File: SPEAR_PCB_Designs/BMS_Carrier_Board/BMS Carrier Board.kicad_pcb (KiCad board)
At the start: 2 copper layers, 2 parts, among them U1 74LV1T08GW

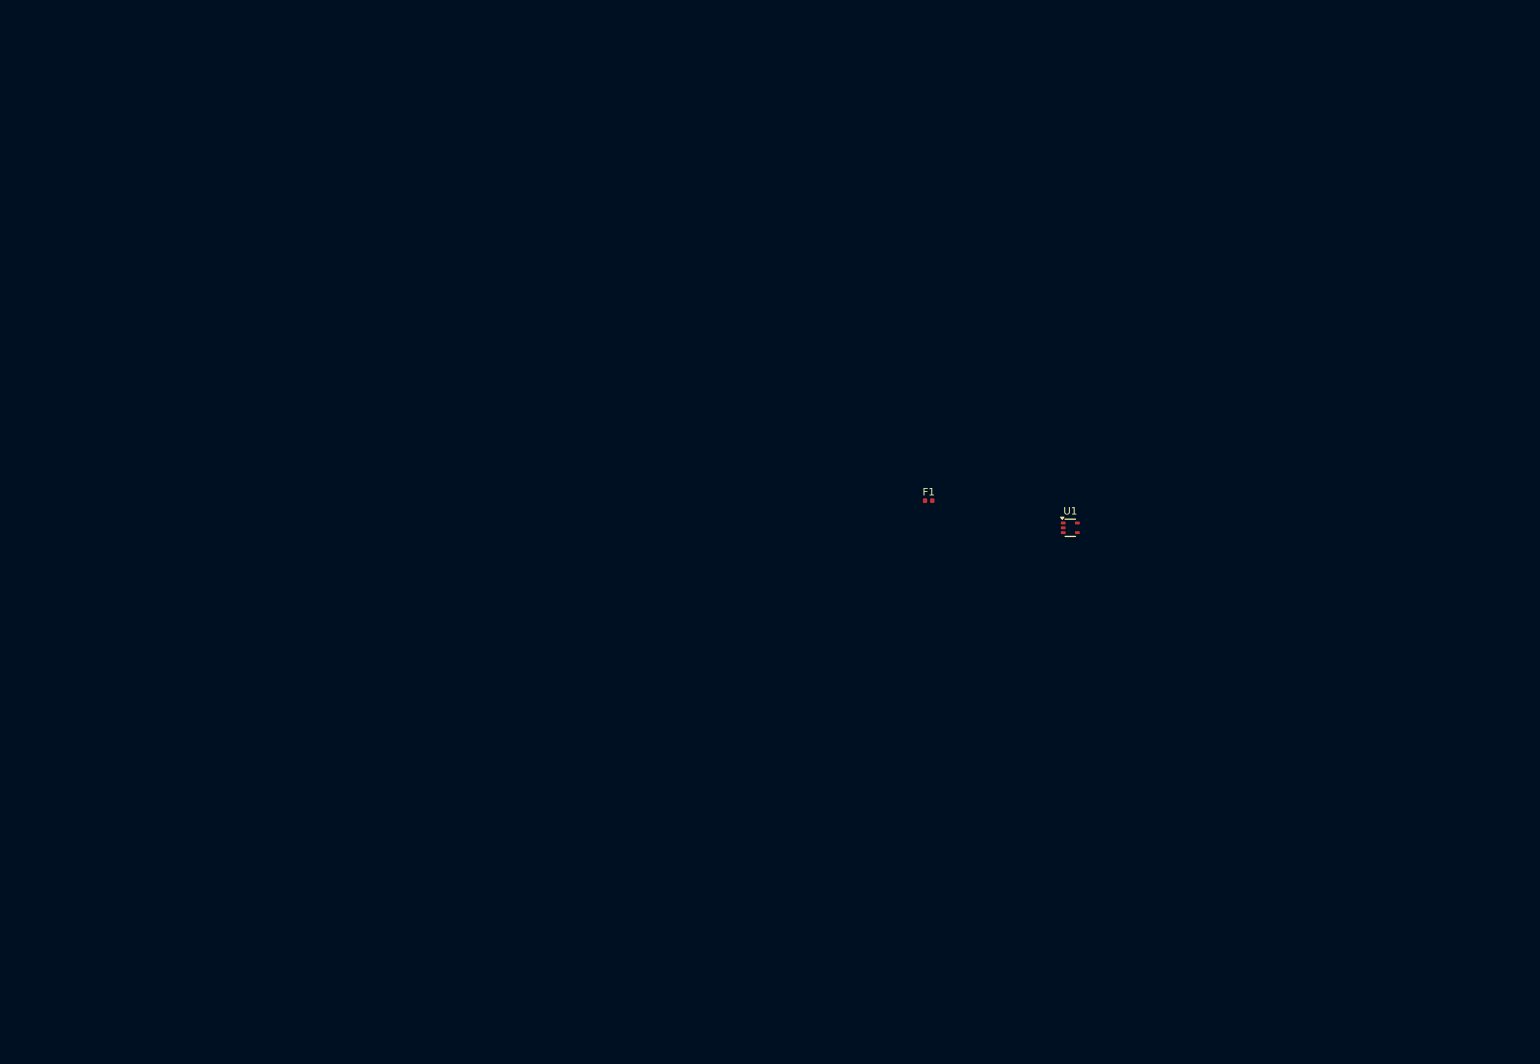
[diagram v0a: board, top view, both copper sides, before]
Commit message: created BMS board schematic
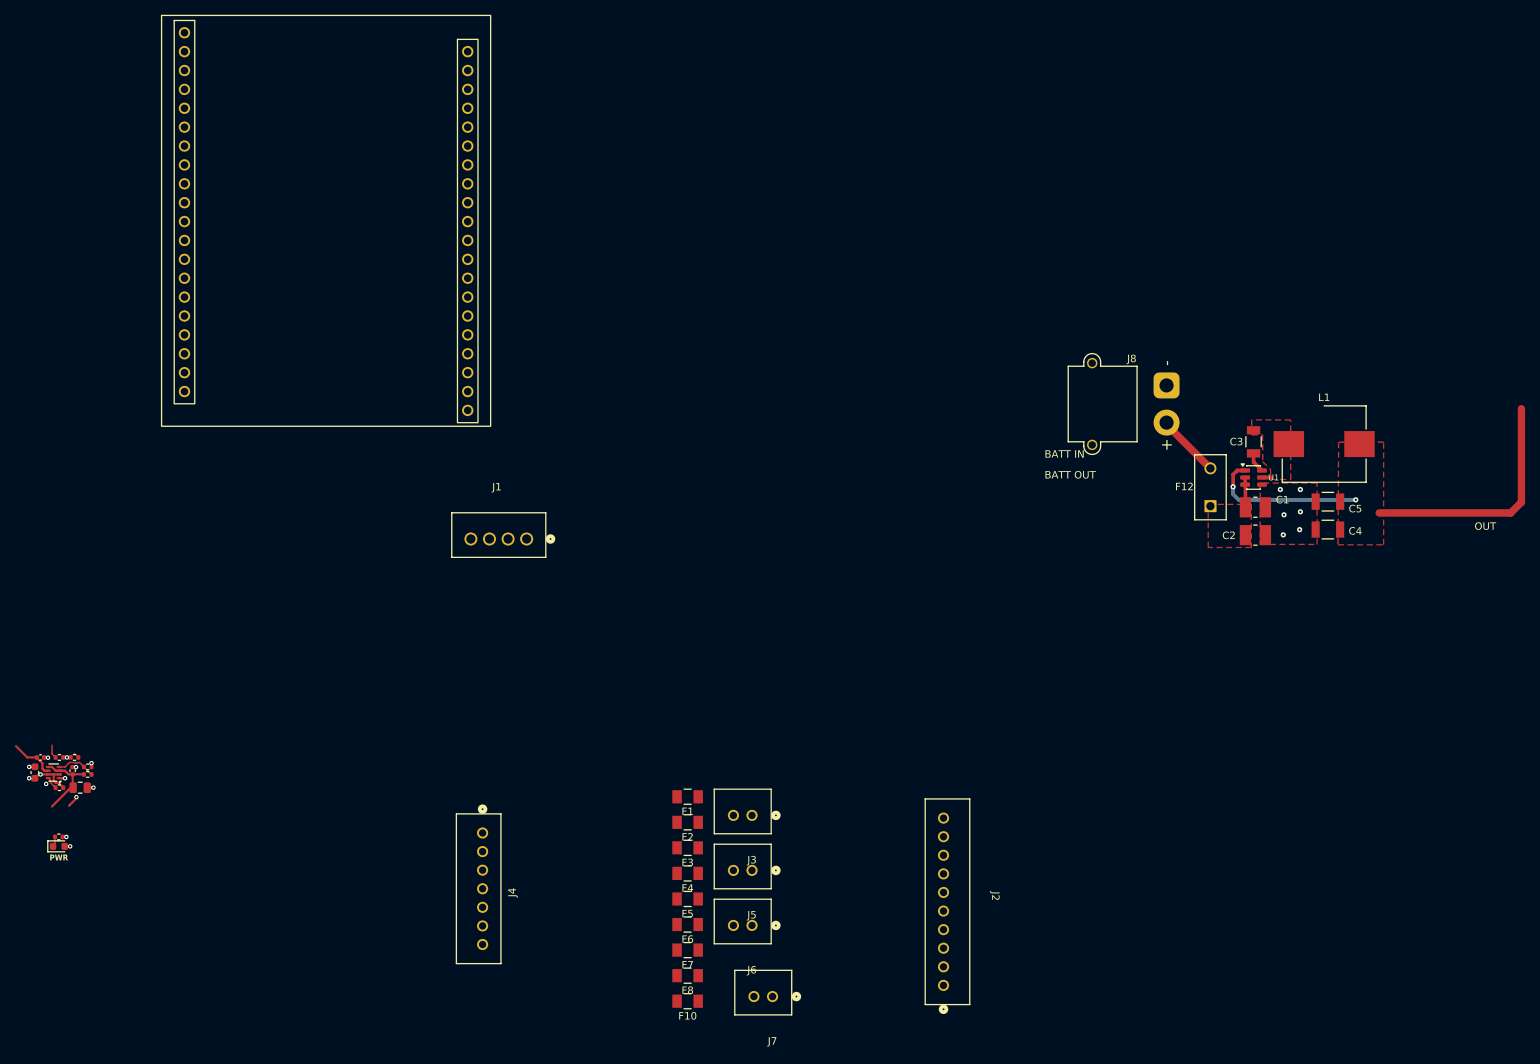
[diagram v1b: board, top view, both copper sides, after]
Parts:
- added C1: 10uF, SPEAR_MotorControllerCarrier:CAPC3225X270N, F.Cu at (197.9, 92.4)
- added C15: 22uF, Capacitor_SMD:C_0805_2012Metric, F.Cu at (39.9, 130.1)
- added C2: 10uF, SPEAR_MotorControllerCarrier:CAPC3225X270N, F.Cu at (197.9, 96.1)
- added C3: 150nF, SPEAR_MotorControllerCarrier:CAP_CC1206_YAG, F.Cu at (197.7, 83.6)
- added C4: 22uF, SPEAR_MotorControllerCarrier:CAP_C3225X7R1C226M250AC, F.Cu at (207.7, 95.4)
- added C5: 22uF, SPEAR_MotorControllerCarrier:CAP_C3225X7R1C226M250AC, F.Cu at (207.7, 91.6)
- added C50: 1uF, Capacitor_SMD:C_0402_1005Metric, F.Cu at (38.9, 127.8)
- added C51: 1uF, Capacitor_SMD:C_0402_1005Metric, F.Cu at (34.5, 126.0)
- added C52: 10uF, Capacitor_SMD:C_0603_1608Metric, F.Cu at (33.8, 128.1)
- added D1: LED_RED, LED_SMD:LED_0603_1608Metric, F.Cu at (37.0, 138.0)
- added F10: C1Q 1.5, BMS footprints:C1_BEL, F.Cu at (121.6, 158.8)
- added F12: 2A, SPEAR_MotorControllerCarrier:FUS_LITTELFUSE_392_LTF, F.Cu at (191.9, 92.2)
- added F2: C1Q 1.5, BMS footprints:C1_BEL, F.Cu at (121.6, 134.8)
- added F3: C1Q 1.5, BMS footprints:C1_BEL, F.Cu at (121.6, 138.2)
- added F4: C1Q 1.5, BMS footprints:C1_BEL, F.Cu at (121.6, 141.6)
- added F5: C1Q 1.5, BMS footprints:C1_BEL, F.Cu at (121.6, 145.1)
- added F6: C1Q 1.5, BMS footprints:C1_BEL, F.Cu at (121.6, 148.5)
- added F7: C1Q 1.5, BMS footprints:C1_BEL, F.Cu at (121.6, 152.0)
- added F8: C1Q 1.5, BMS footprints:C1_BEL, F.Cu at (121.6, 155.4)
- added J1: B4B-XH-A, BMS footprints:CONN_B4B-XH-A_JST, F.Cu at (99.9, 96.7)
- added J2: B10B-XH-A, BMS footprints:CONN_B10B-XH-A_JST, F.Cu at (156.0, 156.7)
- added J3: B2B-XH-A, BMS footprints:CONN_B2B-XH-A_JST, F.Cu at (130.2, 133.8)
- added J4: B7B-XH-A, BMS footprints:CONN_B7B-XH-A_JST, F.Cu at (94.0, 136.2)
- added J5: B2B-XH-A, BMS footprints:CONN_B2B-XH-A_JST, F.Cu at (130.2, 141.2)
- added J6: B2B-XH-A, BMS footprints:CONN_B2B-XH-A_JST, F.Cu at (130.2, 148.6)
- added J7: B2B-XH-A, BMS footprints:CONN_B2B-XH-A_JST, F.Cu at (133.0, 158.2)
- added J8: Conn_01x02_Pin, SPEAR_Connectors:AMASS_XT30PW-M_1x02_P2.50mm_Horizontal_1, F.Cu at (186.0, 76.0)
- added L1: 3.9uH, SPEAR_AP63203BuckConverter:L_Wurth_WE-LHMI-1040_L1, F.Cu at (207.2, 83.9)
- added MCB1: Micro_Controller_Board, SPEAR_Boards:Micro_Controller_Board, F.Cu at (51.0, 26.4)
- added R3: 5.1kR, Resistor_SMD:R_0402_1005Metric, F.Cu at (39.1, 126.0)
- added R32: 7.5kR, Resistor_SMD:R_0402_1005Metric, F.Cu at (40.9, 128.3)
- added R33: 5.1kR, Resistor_SMD:R_0402_1005Metric, F.Cu at (40.9, 127.3)
- added R34: 10kR, Resistor_SMD:R_0402_1005Metric, F.Cu at (37.1, 130.1)
- added R4: 5.1kR, Resistor_SMD:R_0402_1005Metric, F.Cu at (37.1, 126.0)
- added R6: 1kR, Resistor_SMD:R_0402_1005Metric, F.Cu at (37.0, 136.7)
- added U6: TPS2116DRL, Package_TO_SOT_SMD:SOT-583-8, F.Cu at (36.3, 128.1)
- F1: value 2A -> C1Q 1.5; footprint Fuse:Fuse_0402_1005Metric -> BMS footprints:C1_BEL
- U1: value 74LV1T08GW -> AP63203WU; footprint Package_TO_SOT_SMD:SOT-353_SC-70-5 -> SPEAR_MotorControllerCarrier:TSOT-23-6
- moved F1 51.4 mm to (121.6, 131.3)
- moved U1 25.6 mm to (197.7, 88.4)
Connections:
- F1 pad 1: +BATT -> Net-(F1-Pad1)
- U1 pad 1: Emergency Stop Switch -> /3.3V_Battery
- U1 pad 2: Battery Power Switch -> /Schematic/BUCK_PWR
- U1 pad 3: GND -> /Schematic/BUCK_PWR
- U1 pad 4: unconnected-(U1-Y-Pad4) -> GND
- U1 pad 5: VCC -> /Schematic/SW
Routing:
- net /3.3V_Battery: track 0.00 -> 53.6 mm, vias 0 -> 2
- net /STM32F446RC/3.3V_USB: track 0.00 -> 11.4 mm
- net +5V: track 0.00 -> 11.0 mm
- net Net-(J1-Pin_2): track 0.00 -> 8.40 mm
- net +3.3V: track 0.00 -> 7.53 mm, vias 0 -> 3
- net /STM32F446RC/3.3V_Battery: track 0.00 -> 6.17 mm
- net Net-(U6-PR1): track 0.00 -> 5.27 mm
- net /Schematic/BUCK_PWR: track 0.00 -> 4.02 mm
- net GND: track 0.00 -> 3.99 mm, vias 0 -> 16
- net /STM32F446RC/PB4: track 0.00 -> 3.72 mm
- net /Schematic/BST: track 0.00 -> 2.77 mm
- net Net-(J1-CC2): track 0.00 -> 1.85 mm
- net Net-(U6-ST): track 0.00 -> 1.69 mm
- net /STM32F446RC/PWR_LED_K: track 0.00 -> 1.38 mm
- net /Schematic/SW: track 0.00 -> 1.25 mm
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- added copper zone on In2.Cu, net +3.3V
- added copper zone on F.Cu, net /3.3V_Battery
- added copper zone on F.Cu, net /Schematic/BUCK_PWR
- added copper zone on F.Cu, net /Schematic/SW
- added copper zone on F.Cu, net GND
- added copper zone on In1.Cu, net GND
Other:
- copper layers 2 -> 4
- board text added: "BATT IN"
- board text added: "BATT OUT"
- board text added: "OUT"
- board text added: "PWR"
